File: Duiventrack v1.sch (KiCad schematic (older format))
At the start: 21 parts, among them P1 CONN_01X06, U1 MCP1711-SOT23-5, U2 SP-ABZ-G

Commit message: Nieuwe versie, nadat het niet meer goed ging
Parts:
- removed JP2: Jumper_NO_Small, Footprint:SolderJumper_NO, symbol Jumper_NO_Small
- removed TP?: TEST, symbol TEST
- added TP1: TEST, symbol TEST
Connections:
- net +3V3: now also U2.48 (VDD_TCXO)
- net at R5.1, U2.43 (BOOT0): now also TP1.1
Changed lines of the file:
@@
 	1    0    0    -1
 $EndComp
-Text GLabel 3550 3500 2    39   Input ~ 0
+Text GLabel 3600 3500 2    39   Input ~ 0
 MCU_RST
 Text GLabel 8000 2750 0    39   Input ~ 0
@@
 Connection ~ 7550 1650
 Wire Wire Line
-	7750 1800 8050 1800
+	7550 1800 8050 1800
 $Comp
 L C C2
@@
 $EndComp
 $Comp
-L Earth #PWR016
+L Earth #PWR015
 U 1 1 5AD7ED21
 P 2950 3900
-F 0 "#PWR016" H 2950 3650 50  0001 C CNN
+F 0 "#PWR015" H 2950 3650 50  0001 C CNN
 F 1 "Earth" H 2950 3750 50  0001 C CNN
 F 2 "" H 2950 3900 50  0000 C CNN
@@
 $EndComp
 Wire Wire Line
+	2950 3500 3600 3500
+Wire Wire Line
 	3250 3400 3250 4000
 Wire Wire Line
@@
 	2950 3500 2950 3600
 $Comp
-L Earth #PWR017
+L Earth #PWR016
 U 1 1 5AD80891
 P 3700 4600
-F 0 "#PWR017" H 3700 4350 50  0001 C CNN
+F 0 "#PWR016" H 3700 4350 50  0001 C CNN
 F 1 "Earth" H 3700 4450 50  0001 C CNN
 F 2 "" H 3700 4600 50  0000 C CNN
@@
 Wire Wire Line
 	3700 4400 3750 4400
-$Comp
-L Jumper_NO_Small JP2
-U 1 1 5AD7946A
-P 7650 1800
-F 0 "JP2" H 7650 1880 50  0000 C CNN
-F 1 "Jumper_NO_Small" H 7660 1740 50  0000 C CNN
-F 2 "Footprint:SolderJumper_NO" H 7650 1800 50  0001 C CNN
-F 3 "" H 7650 1800 50  0000 C CNN
-	1    7650 1800
-	-1   0    0    1
-$EndComp
 NoConn ~ 10250 1350
 NoConn ~ 10250 1500
@@
 NoConn ~ 8050 2650
 $Comp
-L TEST TP?
-U 1 1 5AE08750
+L TEST TP1
+U 1 1 5AE08B1C
 P 7200 2100
-F 0 "TP?" H 7200 2400 50  0000 C BNN
+F 0 "TP1" H 7200 2400 50  0000 C BNN
 F 1 "TEST" H 7200 2350 50  0000 C CNN
-F 2 "" H 7200 2100 50  0001 C CNN
-F 3 "" H 7200 2100 50  0001 C CNN
+F 2 "" H 7200 2100 50  0000 C CNN
+F 3 "" H 7200 2100 50  0000 C CNN
 	1    7200 2100
 	1    0    0    -1
 $EndComp
 Connection ~ 7200 2200
-Wire Wire Line
-	2950 3500 3550 3500
 $EndSCHEMATC

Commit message: Foodprint testpunt toegevoegd, is alleen een beetje groot.
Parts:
- TP1: footprint (none) -> Measurement_Points:Measurement_Point_Round-SMD-Pad_Small
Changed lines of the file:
@@
 F 0 "TP1" H 7200 2400 50  0000 C BNN
 F 1 "TEST" H 7200 2350 50  0000 C CNN
-F 2 "" H 7200 2100 50  0000 C CNN
+F 2 "Measurement_Points:Measurement_Point_Round-SMD-Pad_Small" H 7200 2100 50  0001 C CNN
 F 3 "" H 7200 2100 50  0000 C CNN
 	1    7200 2100

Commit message: Foutmelding murata component gaat nie weg
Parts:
- removed U2: SP-ABZ-G, Foodprint:Murata_SP-ABZ-G, symbol SP-ABZ-G
- added C?: 2.2pF, Capacitors_SMD:C_0402, symbol C
- added U?: SP-ABZ-G, symbol SP-ABZ-G
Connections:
- net +3V3: now also U?.32 (VREF+), U?.4 (VDD_USB), U?.48 (VDD_TCXO), U?.5 (VDD_MCU), U?.6 (VDD_RF)
- net Earth: now also C?.2, U?.25 (GND), U?.27 (GND), U?.3 (GND), U?.44 (GND), U?.49 (GND), U?.50 (GND), U?.51 (GND), U?.52 (GND), U?.53 (GND), U?.54 (GND), U?.55 (GND), U?.56 (GND), U?.57 (GND), U?.7 (GND)
- net MCU_RST: now also U?.34 (MCU_nRST)
- net SWCLK: now also U?.42 (PA14/SWCLK)
- net SWDIO: now also U?.41 (PA13/SWDIO)
- net Uart_RX: now also U?.18 (PA10/USART1_RX)
- net Uart_TX: now also U?.19 (PA9/USART1_TX)
- net VBat_Measure: now also U?.24 (PA2/ADC2)
- net at AE1.1 (A): now also C?.1, U?.26 (ANT)
- net at R5.1, TP1.1: now also U?.43 (BOOT0)
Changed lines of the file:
@@
 LIBS:valves
 LIBS:Project componenten
+LIBS:Mutara_SP-ABZ-G (1)
 LIBS:Duiventrack v1-cache
 EELAYER 25 0
@@
 Text GLabel 10300 3350 2    39   Input ~ 0
 VBat_Measure
-$Comp
-L SP-ABZ-G U2
-U 1 1 5ACF7027
-P 9150 3350
-F 0 "U2" H 9250 1700 60  0000 C CNN
-F 1 "SP-ABZ-G" H 9150 5500 60  0000 C CNN
-F 2 "Foodprint:Murata_SP-ABZ-G" H 9250 4450 60  0001 C CNN
-F 3 "" H 9250 4450 60  0001 C CNN
-	1    9150 3350
-	1    0    0    -1
-$EndComp
 $Comp
 L Battery_Cell BT1
@@
 $EndComp
 Connection ~ 7200 2200
+$Comp
+L C C?
+U 1 1 5AE853A6
+P 7150 4200
+F 0 "C?" H 7175 4300 50  0000 L CNN
+F 1 "2.2pF" H 7175 4100 50  0000 L CNN
+F 2 "Capacitors_SMD:C_0402" H 7188 4050 50  0001 C CNN
+F 3 "" H 7150 4200 50  0000 C CNN
+	1    7150 4200
+	1    0    0    -1
+$EndComp
+$Comp
+L Earth #PWR?
+U 1 1 5AE85758
+P 7150 4350
+F 0 "#PWR?" H 7150 4100 50  0001 C CNN
+F 1 "Earth" H 7150 4200 50  0001 C CNN
+F 2 "" H 7150 4350 50  0000 C CNN
+F 3 "" H 7150 4350 50  0000 C CNN
+	1    7150 4350
+	1    0    0    -1
+$EndComp
+Wire Wire Line
+	7150 4050 7150 3950
+Connection ~ 7150 3950
+$Comp
+L SP-ABZ-G U?
+U 1 1 5AE85422
+P 9150 3350
+F 0 "U?" H 9250 1700 60  0000 C CNN
+F 1 "SP-ABZ-G" H 9150 5500 60  0000 C CNN
+F 2 "" H 9250 4450 60  0001 C CNN
+F 3 "" H 9250 4450 60  0001 C CNN
+	1    9150 3350
+	1    0    0    -1
+$EndComp
 $EndSCHEMATC

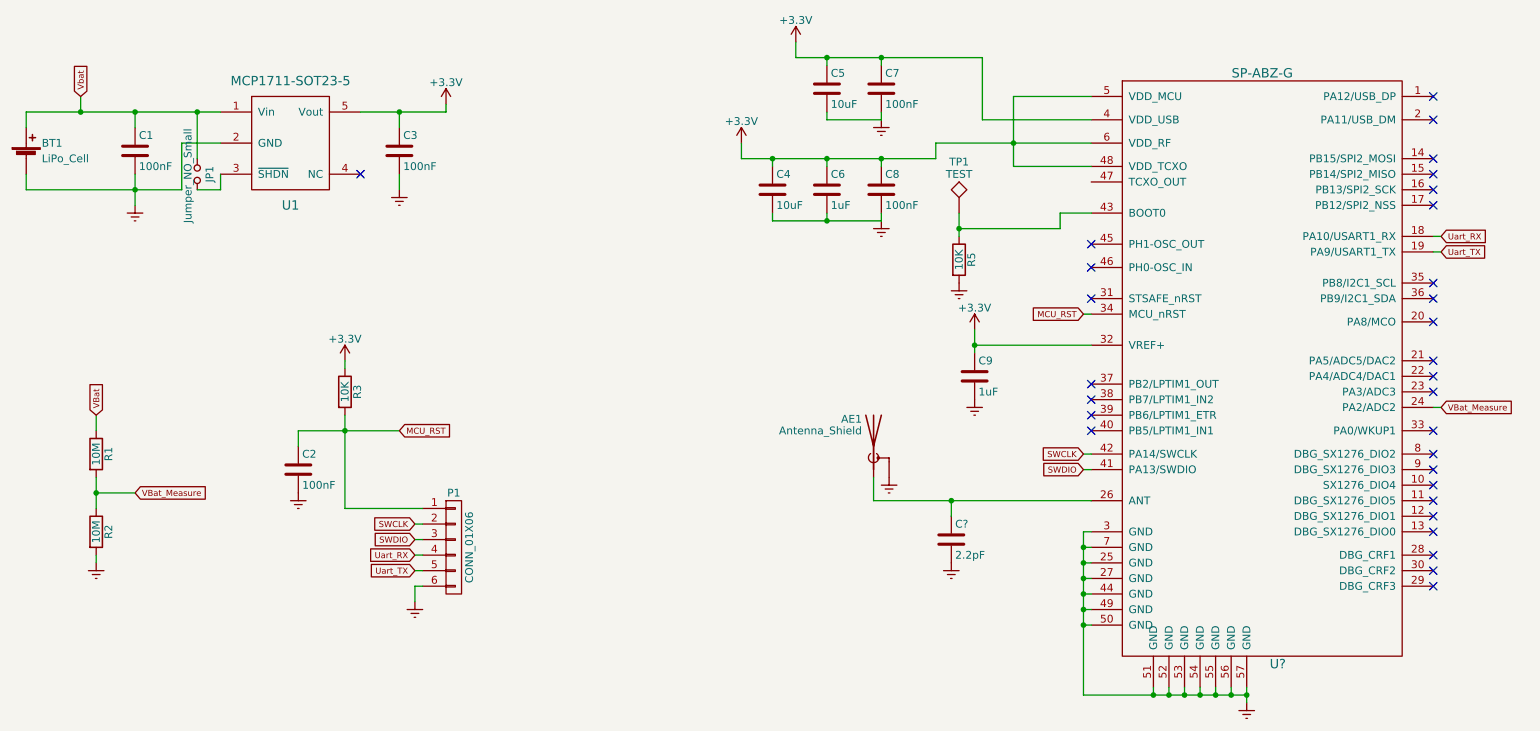
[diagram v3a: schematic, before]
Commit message: Schema afgemaakt en begonnen met de Footprint
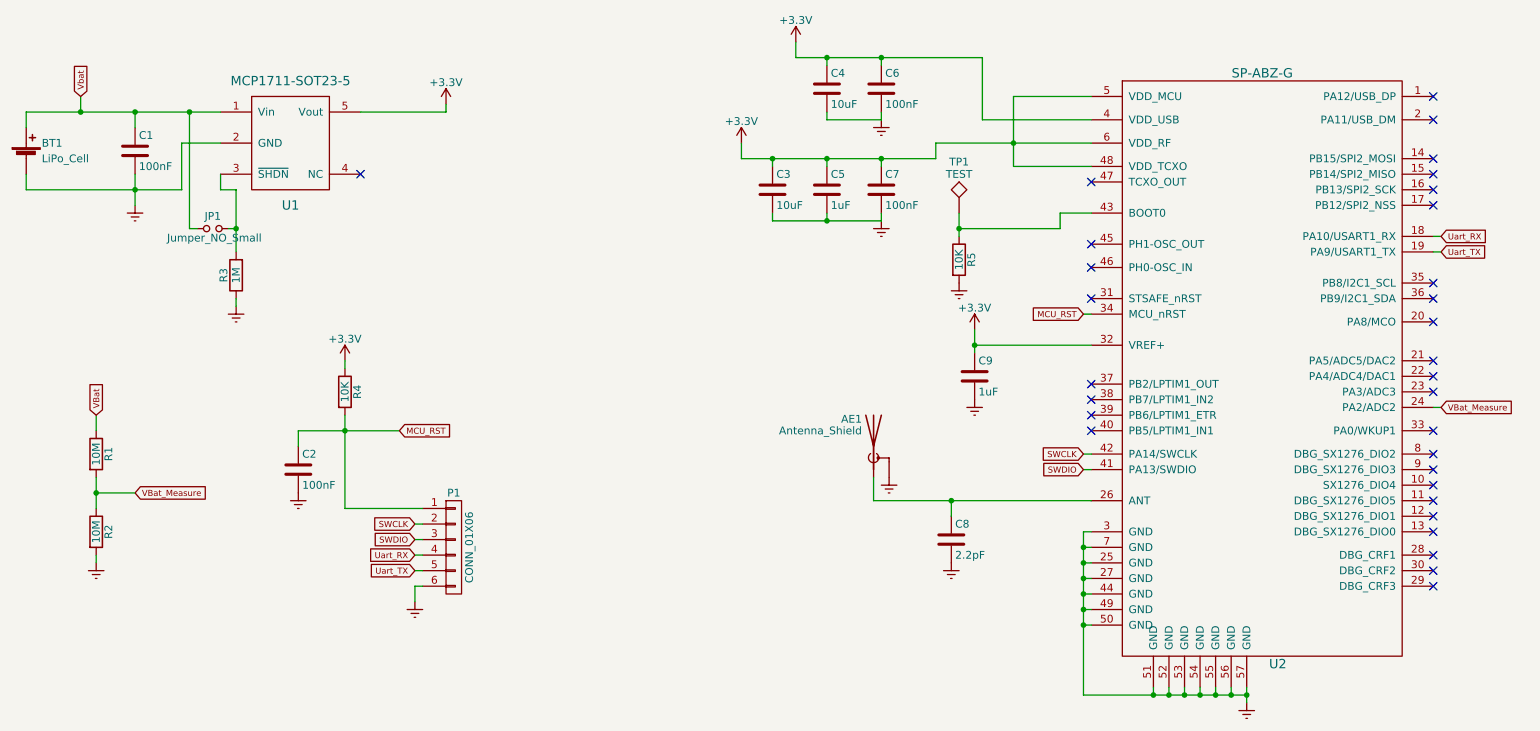
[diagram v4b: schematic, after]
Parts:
- removed C3: 100nF, Capacitors_SMD:C_0402, symbol C
- added R3: 1M, Resistors_SMD:R_0402, symbol R
- BT1: footprint Connectors_JST:JST_SHL_SM02B-SHLS-TF_02x1.00mm_Angled -> Pin_Headers:Pin_Header_Straight_1x02_Pitch1.27mm
- C3: renamed from C4; footprint Capacitors_SMD:C_0603 -> Capacitors_SMD:C_0402
- C4: renamed from C5; footprint Capacitors_SMD:C_0603 -> Capacitors_SMD:C_0402
- P1: footprint Connectors_JAE:JAE_LY20-06P-2T_2x03x2.00mm_Straight -> Pin_Headers:Pin_Header_Straight_1x06_Pitch1.27mm
- U2: renamed from U?; footprint (none) -> Footprint:Murata_SP-ABZ-G
- gave numbers to parts that had none: 1
- renumbered C6 to C5, C7 to C6, C8 to C7, R3 to R4
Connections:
- net Earth: now also R3.1
- net at JP1.2, U1.3 (~SHDN): now also R3.2
- no-connect marks 30 -> 31
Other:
- moved on the sheet: JP1
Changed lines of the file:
@@
 LIBS:valves
 LIBS:Project componenten
-LIBS:Mutara_SP-ABZ-G (1)
 LIBS:Duiventrack v1-cache
 EELAYER 25 0
@@
 $EndDescr
 $Comp
-L C C4
+L C C3
 U 1 1 5AABF48D
 P 6000 1950
-F 0 "C4" H 6025 2050 50  0000 L CNN
+F 0 "C3" H 6025 2050 50  0000 L CNN
 F 1 "10uF" H 6025 1850 50  0000 L CNN
-F 2 "Capacitors_SMD:C_0603" H 6038 1800 50  0001 C CNN
+F 2 "Capacitors_SMD:C_0402" H 6038 1800 50  0001 C CNN
 F 3 "" H 6000 1950 50  0000 C CNN
 	1    6000 1950
@@
 $EndComp
 $Comp
-L C C6
+L C C5
 U 1 1 5AABF792
 P 6350 1950
-F 0 "C6" H 6375 2050 50  0000 L CNN
+F 0 "C5" H 6375 2050 50  0000 L CNN
 F 1 "1uF" H 6375 1850 50  0000 L CNN
 F 2 "Capacitors_SMD:C_0402" H 6388 1800 50  0001 C CNN
@@
 $EndComp
 $Comp
-L C C8
+L C C7
 U 1 1 5AABF7CB
 P 6700 1950
-F 0 "C8" H 6725 2050 50  0000 L CNN
+F 0 "C7" H 6725 2050 50  0000 L CNN
 F 1 "100nF" H 6725 1850 50  0000 L CNN
 F 2 "Capacitors_SMD:C_0402" H 6738 1800 50  0001 C CNN
@@
 $EndComp
 $Comp
-L C C5
+L C C4
 U 1 1 5AABFA33
 P 6350 1300
-F 0 "C5" H 6375 1400 50  0000 L CNN
+F 0 "C4" H 6375 1400 50  0000 L CNN
 F 1 "10uF" H 6375 1200 50  0000 L CNN
-F 2 "Capacitors_SMD:C_0603" H 6388 1150 50  0001 C CNN
+F 2 "Capacitors_SMD:C_0402" H 6388 1150 50  0001 C CNN
 F 3 "" H 6350 1300 50  0000 C CNN
 	1    6350 1300
@@
 $EndComp
 $Comp
-L C C7
+L C C6
 U 1 1 5AABFA7C
 P 6700 1300
-F 0 "C7" H 6725 1400 50  0000 L CNN
+F 0 "C6" H 6725 1400 50  0000 L CNN
 F 1 "100nF" H 6725 1200 50  0000 L CNN
 F 2 "Capacitors_SMD:C_0402" H 6738 1150 50  0001 C CNN
@@
 $EndComp
 $Comp
-L R R3
+L R R4
 U 1 1 5ACD0E66
 P 3250 3250
-F 0 "R3" V 3330 3250 50  0000 C CNN
+F 0 "R4" V 3330 3250 50  0000 C CNN
 F 1 "10K" V 3250 3250 50  0000 C CNN
 F 2 "Resistors_SMD:R_0402" V 3180 3250 50  0001 C CNN
@@
 F 0 "BT1" H 1300 1850 50  0000 L CNN
 F 1 "LiPo_Cell" H 1300 1750 50  0000 L CNN
-F 2 "Connectors_JST:JST_SHL_SM02B-SHLS-TF_02x1.00mm_Angled" V 1200 1810 50  0001 C CNN
+F 2 "Pin_Headers:Pin_Header_Straight_1x02_Pitch1.27mm" V 1200 1810 50  0001 C CNN
 F 3 "" V 1200 1810 50  0000 C CNN
 	1    1200 1750
@@
 $EndComp
 NoConn ~ 3350 1850
-$Comp
-L C C3
-U 1 1 5ACF9510
-P 3600 1700
-F 0 "C3" H 3625 1800 50  0000 L CNN
-F 1 "100nF" H 3625 1600 50  0000 L CNN
-F 2 "Capacitors_SMD:C_0402" H 3638 1550 50  0001 C CNN
-F 3 "" H 3600 1700 50  0000 C CNN
-	1    3600 1700
-	1    0    0    -1
-$EndComp
 $Comp
 L C C1
@@
 	1    0    0    -1
 $EndComp
-$Comp
-L Earth #PWR013
-U 1 1 5ACFB150
-P 3600 1950
-F 0 "#PWR013" H 3600 1700 50  0001 C CNN
-F 1 "Earth" H 3600 1800 50  0001 C CNN
-F 2 "" H 3600 1950 50  0000 C CNN
-F 3 "" H 3600 1950 50  0000 C CNN
-	1    3600 1950
-	1    0    0    -1
-$EndComp
 Text GLabel 1550 1350 1    39   Input ~ 0
 Vbat
 $Comp
-L +3.3V #PWR014
+L +3.3V #PWR013
 U 1 1 5ACFF42A
 P 3900 1400
-F 0 "#PWR014" H 3900 1250 50  0001 C CNN
+F 0 "#PWR013" H 3900 1250 50  0001 C CNN
 F 1 "+3.3V" H 3900 1540 50  0000 C CNN
 F 2 "" H 3900 1400 50  0000 C CNN
@@
 L Jumper_NO_Small JP1
 U 1 1 5AD79D47
-P 2300 1850
-F 0 "JP1" H 2300 1930 50  0000 C CNN
-F 1 "Jumper_NO_Small" H 2310 1790 50  0000 C CNN
-F 2 "Footprint:SolderJumper_NO" H 2300 1850 50  0001 C CNN
-F 3 "" H 2300 1850 50  0000 C CNN
-	1    2300 1850
-	0    1    1    0
+P 2400 2200
+F 0 "JP1" H 2400 2280 50  0000 C CNN
+F 1 "Jumper_NO_Small" H 2410 2140 50  0000 C CNN
+F 2 "Footprint:SolderJumper_NO" H 2400 2200 50  0001 C CNN
+F 3 "" H 2400 2200 50  0000 C CNN
+	1    2400 2200
+	1    0    0    -1
 $EndComp
 Wire Wire Line
@@
 Wire Wire Line
 	7050 1650 7050 1750
-Connection ~ 2300 1450
-Wire Wire Line
-	2300 1750 2300 1450
-Wire Wire Line
-	2450 1950 2300 1950
-Wire Wire Line
-	2450 1850 2450 1950
 Wire Wire Line
 	7850 2100 8050 2100
@@
 Wire Wire Line
 	3350 1450 3900 1450
-Connection ~ 3600 1450
-Wire Wire Line
-	3600 1450 3600 1550
-Wire Wire Line
-	3600 1850 3600 1950
 Wire Wire Line
 	1200 1450 2450 1450
@@
 $EndComp
 $Comp
-L Earth #PWR015
+L Earth #PWR014
 U 1 1 5AD7ED21
 P 2950 3900
-F 0 "#PWR015" H 2950 3650 50  0001 C CNN
+F 0 "#PWR014" H 2950 3650 50  0001 C CNN
 F 1 "Earth" H 2950 3750 50  0001 C CNN
 F 2 "" H 2950 3900 50  0000 C CNN
@@
 	2950 3500 2950 3600
 $Comp
-L Earth #PWR016
+L Earth #PWR015
 U 1 1 5AD80891
 P 3700 4600
-F 0 "#PWR016" H 3700 4350 50  0001 C CNN
+F 0 "#PWR015" H 3700 4350 50  0001 C CNN
 F 1 "Earth" H 3700 4450 50  0001 C CNN
 F 2 "" H 3700 4600 50  0000 C CNN
@@
 F 0 "P1" H 3950 4600 50  0000 C CNN
 F 1 "CONN_01X06" V 4050 4250 50  0000 C CNN
-F 2 "Connectors_JAE:JAE_LY20-06P-2T_2x03x2.00mm_Straight" H 3950 4250 50  0001 C CNN
+F 2 "Pin_Headers:Pin_Header_Straight_1x06_Pitch1.27mm" H 3950 4250 50  0001 C CNN
 F 3 "" H 3950 4250 50  0000 C CNN
 	1    3950 4250
@@
 Connection ~ 7200 2200
 $Comp
-L C C?
+L C C8
 U 1 1 5AE853A6
 P 7150 4200
-F 0 "C?" H 7175 4300 50  0000 L CNN
+F 0 "C8" H 7175 4300 50  0000 L CNN
 F 1 "2.2pF" H 7175 4100 50  0000 L CNN
 F 2 "Capacitors_SMD:C_0402" H 7188 4050 50  0001 C CNN
@@
 $EndComp
 $Comp
-L Earth #PWR?
+L Earth #PWR016
 U 1 1 5AE85758
 P 7150 4350
-F 0 "#PWR?" H 7150 4100 50  0001 C CNN
+F 0 "#PWR016" H 7150 4100 50  0001 C CNN
 F 1 "Earth" H 7150 4200 50  0001 C CNN
 F 2 "" H 7150 4350 50  0000 C CNN
@@
 Connection ~ 7150 3950
 $Comp
-L SP-ABZ-G U?
+L SP-ABZ-G U2
 U 1 1 5AE85422
 P 9150 3350
-F 0 "U?" H 9250 1700 60  0000 C CNN
+F 0 "U2" H 9250 1700 60  0000 C CNN
 F 1 "SP-ABZ-G" H 9150 5500 60  0000 C CNN
-F 2 "" H 9250 4450 60  0001 C CNN
+F 2 "Footprint:Murata_SP-ABZ-G" H 9250 4450 60  0001 C CNN
 F 3 "" H 9250 4450 60  0001 C CNN
 	1    9150 3350
 	1    0    0    -1
 $EndComp
+$Comp
+L R R3
+U 1 1 5AE86CF1
+P 2550 2500
+F 0 "R3" V 2630 2500 50  0000 C CNN
+F 1 "1M" V 2550 2500 50  0000 C CNN
+F 2 "Resistors_SMD:R_0402" V 2480 2500 50  0001 C CNN
+F 3 "" H 2550 2500 50  0000 C CNN
+	1    2550 2500
+	-1   0    0    1
+$EndComp
+$Comp
+L Earth #PWR017
+U 1 1 5AE87323
+P 2550 2700
+F 0 "#PWR017" H 2550 2450 50  0001 C CNN
+F 1 "Earth" H 2550 2550 50  0001 C CNN
+F 2 "" H 2550 2700 50  0000 C CNN
+F 3 "" H 2550 2700 50  0000 C CNN
+	1    2550 2700
+	1    0    0    -1
+$EndComp
+Wire Wire Line
+	2450 1850 2450 1950
+Wire Wire Line
+	2450 1950 2550 1950
+Wire Wire Line
+	2550 1950 2550 2350
+Wire Wire Line
+	2550 2200 2500 2200
+Wire Wire Line
+	2550 2650 2550 2700
+Connection ~ 2550 2200
+Wire Wire Line
+	2300 2200 2250 2200
+Wire Wire Line
+	2250 2200 2250 1450
+Connection ~ 2250 1450
+NoConn ~ 8050 1900
 $EndSCHEMATC
